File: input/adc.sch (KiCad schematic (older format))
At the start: 16 parts, among them U101 LTC2512-24

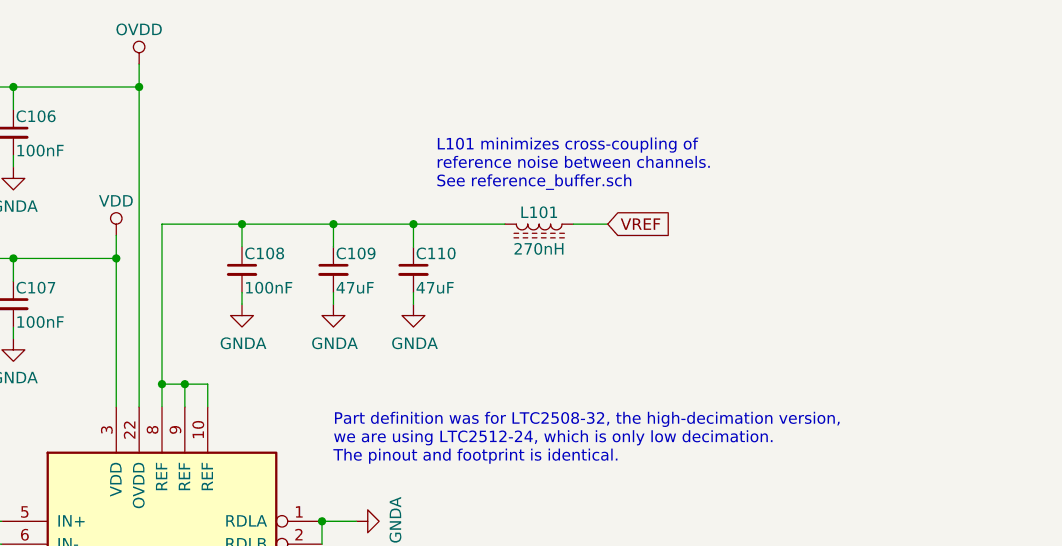
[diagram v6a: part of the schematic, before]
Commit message: Mostly work on power, regulators and distribution.  Also more BOM cleanup.
All of the bypass capacitors are now spec'd and in the DigiKey BOM. TVS zeners are now
spec'd.  Folded together some resistor values and got rid of some 1206 parts that no longer
need that much power rating at the lower supplies.

A affecting all of the input channel sheets is that we now distribute filtered V+, V- and VREF
via sheet ports.  The V+, V- filter is on input_channel.sch and the VREF filter is still in
adc.sch, but is distributed out to the other sheets that need it.

bist_buffer.sch: added buffer for built-in self-test

board_connector.sch: put the input filter for the analog supplies here.

power.sch: added regulators for the supplies.

reference_buffer.sch:
changed components to match those chosen for the V+, V- regulators and added
current steering diodes to bootstrap the reference buffer supply.  This is
necessary because the analog supplies are now derived from VREF.

*.wxsch:
Updates to spice models related to work on supplies.
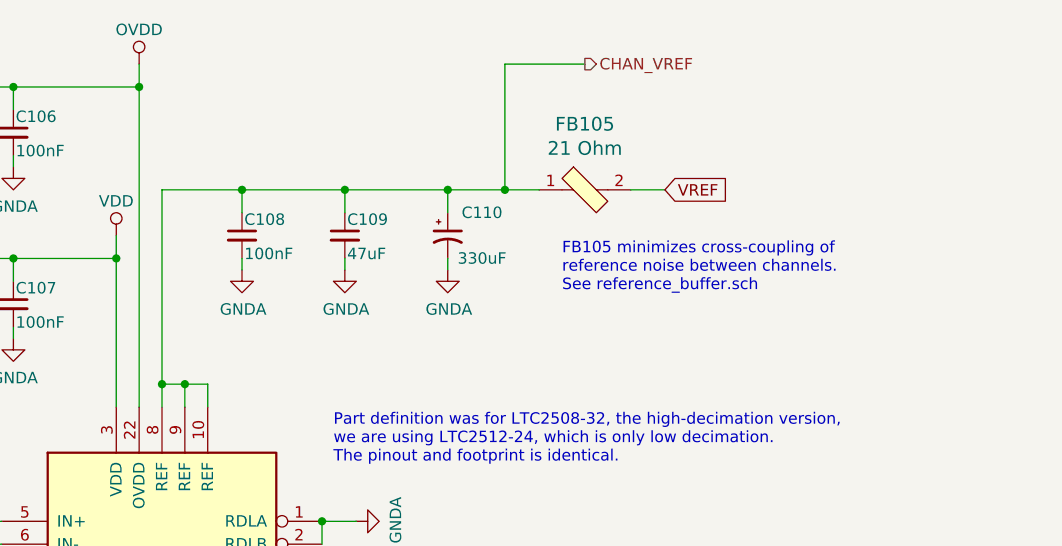
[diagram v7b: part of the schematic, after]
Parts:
- removed C110: 47uF, Capacitor_SMD:C_1210_3225Metric, symbol Device:C_Small
- removed L101: 270nH, Inductor_SMD:L_0603_1608Metric, symbol Device:L_Core_Ferrite
- added C110: 330uF, Capacitor_SMD:CP_Elec_8x6.7, symbol Device:CP1_Small
- added FB105: 21 Ohm, digikey-footprints:0805, symbol dk_Ferrite-Beads-and-Chips:MPZ2012S601AT000
- C104, C105: Description (none) -> CAP CER 10UF 6.3V X5R 0603; Digikey (none) -> 478-5318-1-ND; MPN (none) -> 06036D106MAT2A
- C109: Description (none) -> CAP CER 47UF 6.3V X7R 1210; Digikey (none) -> 399-5516-1-ND; MPN (none) -> C1210C476M9RACTU
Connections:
- net GNDA: now also C110.2
- net VREF: now also FB105.2
- net CHAN_VREF: now reaches C108.1, C109.1, U101.10 (REF), U101.8 (REF), U101.9 (REF)
- net CHAN_VREF: now also C110.1, FB105.1
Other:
- note added: "FB105 minimizes cross-coupling of \nreference noise between channels.\nSee reference_buffer.sch"
- note removed: "L101 minimizes cross-coupling of \nreference noise between channels.\nSee reference_buffer.sch"
- moved on the sheet: C108, C109
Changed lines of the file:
@@
 EESchema Schematic File Version 4
 LIBS:input_board-cache
-LIBS:input_channel-cache
-LIBS:reference_buffer-cache
 EELAYER 29 0
 EELAYER END
 $Descr A4 11693 8268
 encoding utf-8
-Sheet 3 11
+Sheet 6 12
 Title ""
 Date ""
@@
 	1    0    0    -1
 $EndComp
-Text GLabel 8850 2300 2    50   Input ~ 0
+Text GLabel 9100 2150 2    50   Input ~ 0
 VREF
 Wire Wire Line
@@
 Connection ~ 7000 3000
 $Comp
-L Device:C_Small C110
-U 1 1 5E1955C5
-P 8000 2500
-F 0 "C110" H 8010 2570 50  0000 L CNN
-F 1 "47uF" H 8010 2420 50  0000 L CNN
-F 2 "Capacitor_SMD:C_1210_3225Metric" H 8000 2500 50  0001 C CNN
-F 3 "~" H 8000 2500 50  0001 C CNN
-	1    8000 2500
-	1    0    0    -1
-$EndComp
-$Comp
 L power:GNDA #PWR?
 U 1 1 5E1955C6
-P 8000 2650
+P 8150 2500
 AR Path="/5E1955C6" Ref="#PWR?"  Part="1"
 AR Path="/5DA78AA2/5E1955C6" Ref="#PWR?"  Part="1"
 AR Path="/5DFCF14D/5DA78AA2/5E1955C6" Ref="#PWR0114"  Part="1"
-F 0 "#PWR0114" H 8000 2400 50  0001 C CNN
-F 1 "GNDA" H 8005 2477 50  0000 C CNN
-F 2 "" H 8000 2650 50  0001 C CNN
-F 3 "" H 8000 2650 50  0001 C CNN
-	1    8000 2650
-	1    0    0    -1
-$EndComp
-Wire Wire Line
-	8000 2650 8000 2600
-Wire Wire Line
-	8000 2400 8000 2300
-Connection ~ 8000 2300
-Wire Wire Line
-	8000 2300 7650 2300
-Wire Wire Line
-	6900 2300 6900 3000
+F 0 "#PWR0114" H 8150 2250 50  0001 C CNN
+F 1 "GNDA" H 8155 2327 50  0000 C CNN
+F 2 "" H 8150 2500 50  0001 C CNN
+F 3 "" H 8150 2500 50  0001 C CNN
+	1    8150 2500
+	1    0    0    -1
+$EndComp
+Wire Wire Line
+	8150 2250 8150 2150
 $Comp
 L Device:C_Small C109
 U 1 1 5E1955C7
-P 7650 2500
-F 0 "C109" H 7660 2570 50  0000 L CNN
-F 1 "47uF" H 7660 2420 50  0000 L CNN
-F 2 "Capacitor_SMD:C_1210_3225Metric" H 7650 2500 50  0001 C CNN
-F 3 "~" H 7650 2500 50  0001 C CNN
-	1    7650 2500
+P 7700 2350
+F 0 "C109" H 7710 2420 50  0000 L CNN
+F 1 "47uF" H 7710 2270 50  0000 L CNN
+F 2 "Capacitor_SMD:C_1210_3225Metric" H 7700 2350 50  0001 C CNN
+F 3 "https://api.kemet.com/component-edge/download/datasheet/C1210C476M9RACTU.pdf" H 7700 2350 50  0001 C CNN
+F 4 "CAP CER 47UF 6.3V X7R 1210" H 7700 2350 50  0001 C CNN "Description"
+F 5 "399-5516-1-ND" H 7700 2350 50  0001 C CNN "Digikey"
+F 6 "C1210C476M9RACTU" H 7700 2350 50  0001 C CNN "MPN"
+	1    7700 2350
 	1    0    0    -1
 $EndComp
@@
 L power:GNDA #PWR?
 U 1 1 5E1955C8
-P 7650 2650
+P 7700 2500
 AR Path="/5E1955C8" Ref="#PWR?"  Part="1"
 AR Path="/5DA78AA2/5E1955C8" Ref="#PWR?"  Part="1"
 AR Path="/5DFCF14D/5DA78AA2/5E1955C8" Ref="#PWR0112"  Part="1"
-F 0 "#PWR0112" H 7650 2400 50  0001 C CNN
-F 1 "GNDA" H 7655 2477 50  0000 C CNN
-F 2 "" H 7650 2650 50  0001 C CNN
-F 3 "" H 7650 2650 50  0001 C CNN
-	1    7650 2650
-	1    0    0    -1
-$EndComp
-Wire Wire Line
-	7650 2650 7650 2600
-Wire Wire Line
-	7650 2400 7650 2300
+F 0 "#PWR0112" H 7700 2250 50  0001 C CNN
+F 1 "GNDA" H 7705 2327 50  0000 C CNN
+F 2 "" H 7700 2500 50  0001 C CNN
+F 3 "" H 7700 2500 50  0001 C CNN
+	1    7700 2500
+	1    0    0    -1
+$EndComp
+Wire Wire Line
+	7700 2500 7700 2450
+Wire Wire Line
+	7700 2250 7700 2150
 $Comp
 L Device:C_Small C105
@@
 F 1 "10uF" H 5910 2570 50  0000 L CNN
 F 2 "Capacitor_SMD:C_0603_1608Metric" H 5900 2650 50  0001 C CNN
-F 3 "~" H 5900 2650 50  0001 C CNN
+F 3 "http://datasheets.avx.com/cx5r.pdf" H 5900 2650 50  0001 C CNN
+F 4 "CAP CER 10UF 6.3V X5R 0603" H 5900 2650 50  0001 C CNN "Description"
+F 5 "478-5318-1-ND" H 5900 2650 50  0001 C CNN "Digikey"
+F 6 "06036D106MAT2A" H 5900 2650 50  0001 C CNN "MPN"
 	1    5900 2650
 	1    0    0    -1
@@
 F 1 "10uF" H 5910 1820 50  0000 L CNN
 F 2 "Capacitor_SMD:C_0603_1608Metric" H 5900 1900 50  0001 C CNN
-F 3 "~" H 5900 1900 50  0001 C CNN
+F 3 "http://datasheets.avx.com/cx5r.pdf" H 5900 1900 50  0001 C CNN
+F 4 "CAP CER 10UF 6.3V X5R 0603" H 5900 1900 50  0001 C CNN "Description"
+F 5 "478-5318-1-ND" H 5900 1900 50  0001 C CNN "Digikey"
+F 6 "06036D106MAT2A" H 5900 1900 50  0001 C CNN "MPN"
 	1    5900 1900
 	1    0    0    -1
@@
 L Device:C_Small C108
 U 1 1 5E1955D1
+P 7250 2350
+F 0 "C108" H 7260 2420 50  0000 L CNN
+F 1 "100nF" H 7260 2270 50  0000 L CNN
+F 2 "Capacitor_SMD:C_0603_1608Metric" H 7250 2350 50  0001 C CNN
+F 3 "~" H 7250 2350 50  0001 C CNN
+	1    7250 2350
+	1    0    0    -1
+$EndComp
+$Comp
+L power:GNDA #PWR?
+U 1 1 5E1955D2
 P 7250 2500
-F 0 "C108" H 7260 2570 50  0000 L CNN
-F 1 "100nF" H 7260 2420 50  0000 L CNN
-F 2 "Capacitor_SMD:C_0603_1608Metric" H 7250 2500 50  0001 C CNN
-F 3 "~" H 7250 2500 50  0001 C CNN
-	1    7250 2500
-	1    0    0    -1
-$EndComp
-$Comp
-L power:GNDA #PWR?
-U 1 1 5E1955D2
-P 7250 2650
 AR Path="/5E1955D2" Ref="#PWR?"  Part="1"
 AR Path="/5DA78AA2/5E1955D2" Ref="#PWR?"  Part="1"
 AR Path="/5DFCF14D/5DA78AA2/5E1955D2" Ref="#PWR0111"  Part="1"
-F 0 "#PWR0111" H 7250 2400 50  0001 C CNN
-F 1 "GNDA" H 7255 2477 50  0000 C CNN
-F 2 "" H 7250 2650 50  0001 C CNN
-F 3 "" H 7250 2650 50  0001 C CNN
-	1    7250 2650
-	1    0    0    -1
-$EndComp
-Wire Wire Line
-	7250 2650 7250 2600
-Wire Wire Line
-	7250 2400 7250 2300
-Connection ~ 7250 2300
-Wire Wire Line
-	7250 2300 6900 2300
-Connection ~ 7650 2300
-Wire Wire Line
-	7250 2300 7650 2300
+F 0 "#PWR0111" H 7250 2250 50  0001 C CNN
+F 1 "GNDA" H 7255 2327 50  0000 C CNN
+F 2 "" H 7250 2500 50  0001 C CNN
+F 3 "" H 7250 2500 50  0001 C CNN
+	1    7250 2500
+	1    0    0    -1
+$EndComp
+Wire Wire Line
+	7250 2500 7250 2450
+Wire Wire Line
+	7250 2250 7250 2150
+Connection ~ 7250 2150
+Wire Wire Line
+	7250 2150 6900 2150
 Wire Wire Line
 	6700 2350 6700 2450
@@
 Wire Bus Line
 	5450 4000 5450 5700
-$Comp
-L Device:L_Core_Ferrite L101
-U 1 1 5E2E1824
-P 8550 2300
-F 0 "L101" V 8500 2300 50  0000 C CNN
-F 1 "270nH" V 8660 2300 50  0000 C CNN
-F 2 "Inductor_SMD:L_0603_1608Metric" H 8550 2300 50  0001 C CNN
-F 3 "https://product.tdk.com/info/en/catalog/datasheets/inductor_commercial_standard_mlj1608_en.pdf" H 8550 2300 50  0001 C CNN
-F 4 "MLJ1608WR27JT000" V 8550 2300 50  0001 C CNN "MPN"
-F 5 "445-174189-1-ND" H 8550 2300 50  0001 C CNN "Digikey"
-	1    8550 2300
-	0    1    1    0
-$EndComp
-Wire Wire Line
-	8000 2300 8400 2300
-Wire Wire Line
-	8700 2300 8850 2300
-Text Notes 8100 2150 0    50   ~ 0
-L101 minimizes cross-coupling of \nreference noise between channels.\nSee reference_buffer.sch
+Text Notes 8650 2600 0    50   ~ 0
+FB105 minimizes cross-coupling of \nreference noise between channels.\nSee reference_buffer.sch
+$Comp
+L dk_Ferrite-Beads-and-Chips:MPZ2012S601AT000 FB?
+U 1 1 5E24DC2D
+P 8750 2150
+AR Path="/5DFCF14D/5DE42731/5E24DC2D" Ref="FB?"  Part="1"
+AR Path="/5DFCF14D/5E24DC2D" Ref="FB?"  Part="1"
+AR Path="/5DFCF14D/5DA78AA2/5E24DC2D" Ref="FB105"  Part="1"
+F 0 "FB105" H 8750 2437 60  0000 C CNN
+F 1 "21 Ohm" H 8750 2331 60  0000 C CNN
+F 2 "digikey-footprints:0805" H 8950 2350 60  0001 L CNN
+F 3 "https://www.yuden.co.jp/productdata/catalog/chipbeads01_e.pdf" H 8950 2450 60  0001 L CNN
+F 4 "HZ0805C202R-10" H 8950 2650 60  0001 L CNN "MPN"
+F 5 "Ferrite Beads and Chips" H 8950 2850 60  0001 L CNN "Family"
+F 6 "FERRITE BEAD 21 OHM 0805, 100 nH, 5 mOhm" H 8950 3150 60  0001 L CNN "Description"
+F 7 "587-1765-1-ND" H 8750 2150 50  0001 C CNN "Digikey"
+	1    8750 2150
+	1    0    0    -1
+$EndComp
+Wire Wire Line
+	8950 2150 9100 2150
+Wire Wire Line
+	6900 2150 6900 3000
+Wire Wire Line
+	8150 2500 8150 2450
+Connection ~ 7700 2150
+Wire Wire Line
+	7700 2150 8150 2150
+Wire Wire Line
+	7250 2150 7700 2150
+Connection ~ 8150 2150
+Wire Wire Line
+	8150 2150 8400 2150
+$Comp
+L Device:CP1_Small C?
+U 1 1 5E2551B7
+P 8150 2350
+AR Path="/5DFF6C0D/5E2551B7" Ref="C?"  Part="1"
+AR Path="/5E1D6729/5E1DA2AA/5E2551B7" Ref="C?"  Part="1"
+AR Path="/5E2EB92B/5E2551B7" Ref="C?"  Part="1"
+AR Path="/5E51E83D/5E2551B7" Ref="C?"  Part="1"
+AR Path="/5DFCF14D/5E2551B7" Ref="C?"  Part="1"
+AR Path="/5DFCF14D/5DA78AA2/5E2551B7" Ref="C110"  Part="1"
+F 0 "C110" H 8300 2450 50  0000 C CNN
+F 1 "330uF" H 8300 2250 50  0000 C CNN
+F 2 "Capacitor_SMD:CP_Elec_8x6.7" H 8150 2350 50  0001 C CNN
+F 3 "~" H 8150 2350 50  0001 C CNN
+F 4 "16V aluminum solid polymer, ESR 22 mOhm" H 8150 2350 50  0001 C CNN "Description"
+F 5 "565-4285-1-ND" H 8150 2350 50  0001 C CNN "Digikey"
+F 6 "APXG160ARA331MH70G" H 8150 2350 50  0001 C CNN "MPN"
+	1    8150 2350
+	1    0    0    -1
+$EndComp
+Text HLabel 8750 1600 2    50   Output ~ 0
+CHAN_VREF
+Wire Wire Line
+	8750 1600 8400 1600
+Connection ~ 8400 2150
+Wire Wire Line
+	8400 1600 8400 2150
+Wire Wire Line
+	8400 2150 8550 2150
 Wire Bus Line
 	5450 5700 8950 5700
